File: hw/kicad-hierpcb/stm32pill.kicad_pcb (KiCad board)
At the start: 2 copper layers, 12 parts, among them U1 STM32F103C8T6

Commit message: kicad-libs/ribbon
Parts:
- moved PC 5.08 mm to (43.2, 71.1)
- moved PD 2.54 mm to (38.1, 71.1)
- moved SWD 2.54 mm to (27.9, 71.1)
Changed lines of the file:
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@@
 	(footprint "Connector_PinHeader_2.54mm:PinHeader_1x03_P2.54mm_Vertical"
 		(layer "F.Cu")
-		(at 38.1 71.12 180)
+		(at 43.18 71.12 180)
 		(descr "Through hole straight pin header, 1x03, 2.54mm pitch, single row")
 		(tags "Through hole pin header THT 1x03 2.54mm single row")
@@
 		(descr "plated through hole")
 		(property "Reference" "NRST"
-			(at -0.635 1.905 0)
+			(at -2.54 0 0)
 			(unlocked yes)
 			(layer "F.SilkS")
@@
 	(footprint "Connector_PinHeader_2.54mm:PinHeader_1x02_P2.54mm_Vertical"
 		(layer "F.Cu")
-		(at 30.48 71.12 180)
+		(at 27.94 71.12 180)
 		(descr "Through hole straight pin header, 1x02, 2.54mm pitch, single row")
 		(tags "Through hole pin header THT 1x02 2.54mm single row")
@@
 		(fp_arc
 			(start -3.379999 4.06)
-			(mid -3.394989 4.460188)
+			(mid -3.394993 4.460187)
 			(end -3.390027 4.05975)
 			(stroke
@@
 		)
 		(property "Value" "I2C_2"
-			(at 0 4.87 360)
+			(at 0 4.87 0)
 			(layer "F.Fab")
 			(effects
@@
 	(footprint "Connector_PinHeader_2.54mm:PinHeader_1x02_P2.54mm_Vertical"
 		(layer "F.Cu")
-		(at 40.64 71.12 180)
+		(at 38.1 71.12 180)
 		(descr "Through hole straight pin header, 1x02, 2.54mm pitch, single row")
 		(tags "Through hole pin header THT 1x02 2.54mm single row")

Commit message: ide stm
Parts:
- removed ADC: ADC0, base:PTH
- removed AL: Arduino Left Pins, Connector_PinHeader_2.54mm:PinHeader_1x15_P2.54mm_Vertical
- removed AR: Arduino Right Pins, Connector_PinHeader_2.54mm:PinHeader_1x15_P2.54mm_Vertical
- removed B0: Boot0, base:PTH
- removed I2C_2: I2C_2, Connector_PinHeader_2.54mm:PinHeader_1x02_P2.54mm_Vertical
- removed NRST: NRST, base:PTH
- removed PC: PC, Connector_PinHeader_2.54mm:PinHeader_1x03_P2.54mm_Vertical
- removed PD: PD, Connector_PinHeader_2.54mm:PinHeader_1x02_P2.54mm_Vertical
- removed SWD: SWD, Connector_PinHeader_2.54mm:PinHeader_1x02_P2.54mm_Vertical
- removed U1: STM32F103C8T6, jlcpcb:LQFP-48_L7.0-W7.0-P0.50-LS9.0-BL
- removed USB: USB, Connector_PinHeader_2.54mm:PinHeader_1x02_P2.54mm_Vertical
- removed Vb: VBAT, base:PTH
- added 3V3 B0 Gnd: B0 Jumper, base:3x PTH 1.7mm, F.Cu at (35.6, 61.0)
- added C1: CL21B103KBANNNC, jlcpcb:C0805, F.Cu at (42.2, 52.6)
- added C2: CL21B103KBANNNC, jlcpcb:C0805, F.Cu at (36.4, 45.0)
- added C3: CL21B103KBANNNC, jlcpcb:C0805, F.Cu at (28.6, 49.9)
- added C4: CL21B103KBANNNC, jlcpcb:C0805, F.Cu at (34.0, 58.7)
- added J1: IDE STM CD, ribbon:IDE STM CD, F.Cu at (25.4, 25.4)
- added J2: IDE STM AB, ribbon:IDE STM AB, F.Cu at (45.7, 25.4)
- added U4: STM32F103C8T6, jlcpcb:LQFP-48_L7.0-W7.0-P0.50-LS9.0-BL, F.Cu at (35.3, 51.6)
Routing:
- net +3.3V: track 0.00 -> 82.4 mm, vias 0 -> 2
- net unconnected-(J1-IDE3_STM43-PadVBusSense): track 0.00 -> 32.4 mm, vias 0 -> 2
- net unconnected-(J2-IDE4_STM22-PadB0): track 0.00 -> 23.0 mm
- net unconnected-(J1-IDE39_STM46-PadSDA): track 0.00 -> 21.2 mm
- net unconnected-(J2-IDE6_STM21-PadB1): track 0.00 -> 20.7 mm
- net unconnected-(J1-IDE5_STM25-PadC0): track 0.00 -> 19.9 mm
- net unconnected-(J1-IDE37_STM45-PadSCL): track 0.00 -> 18.8 mm
- net unconnected-(J2-IDE8_STM20-PadB2): track 0.00 -> 18.4 mm
- net unconnected-(J1-IDE7_STM26-PadC1): track 0.00 -> 17.5 mm
- net unconnected-(J1-IDE35_STM42-PadD7): track 0.00 -> 16.9 mm
- net GND: track 0.00 -> 16.6 mm, vias 0 -> 2
- net unconnected-(J2-IDE10_STM19-PadB3): track 0.00 -> 16.0 mm
- net unconnected-(J1-IDE9_STM27-PadC2): track 0.00 -> 15.2 mm
- net unconnected-(J1-IDE33_STM41-PadD6): track 0.00 -> 14.6 mm
- net unconnected-(J2-IDE12_STM18-PadB4): track 0.00 -> 13.7 mm
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
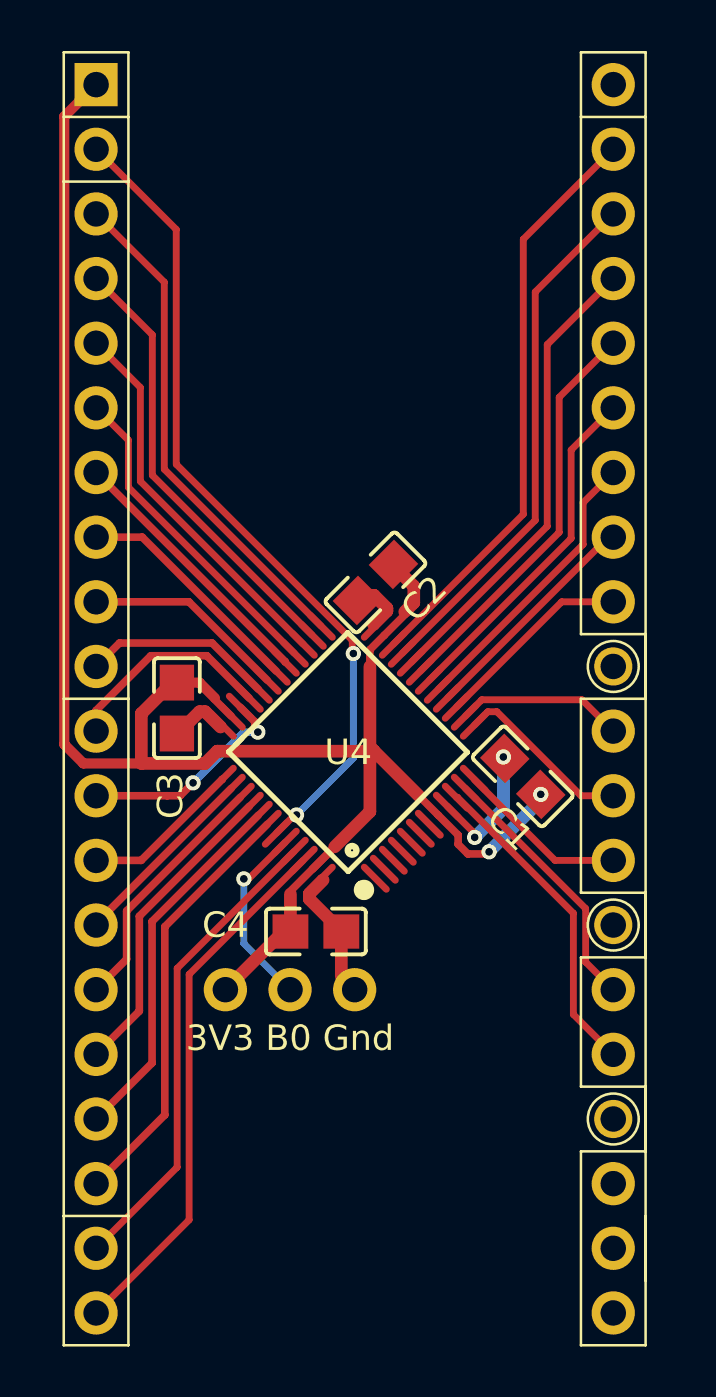
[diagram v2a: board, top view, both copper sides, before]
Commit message: stm32pill pcb
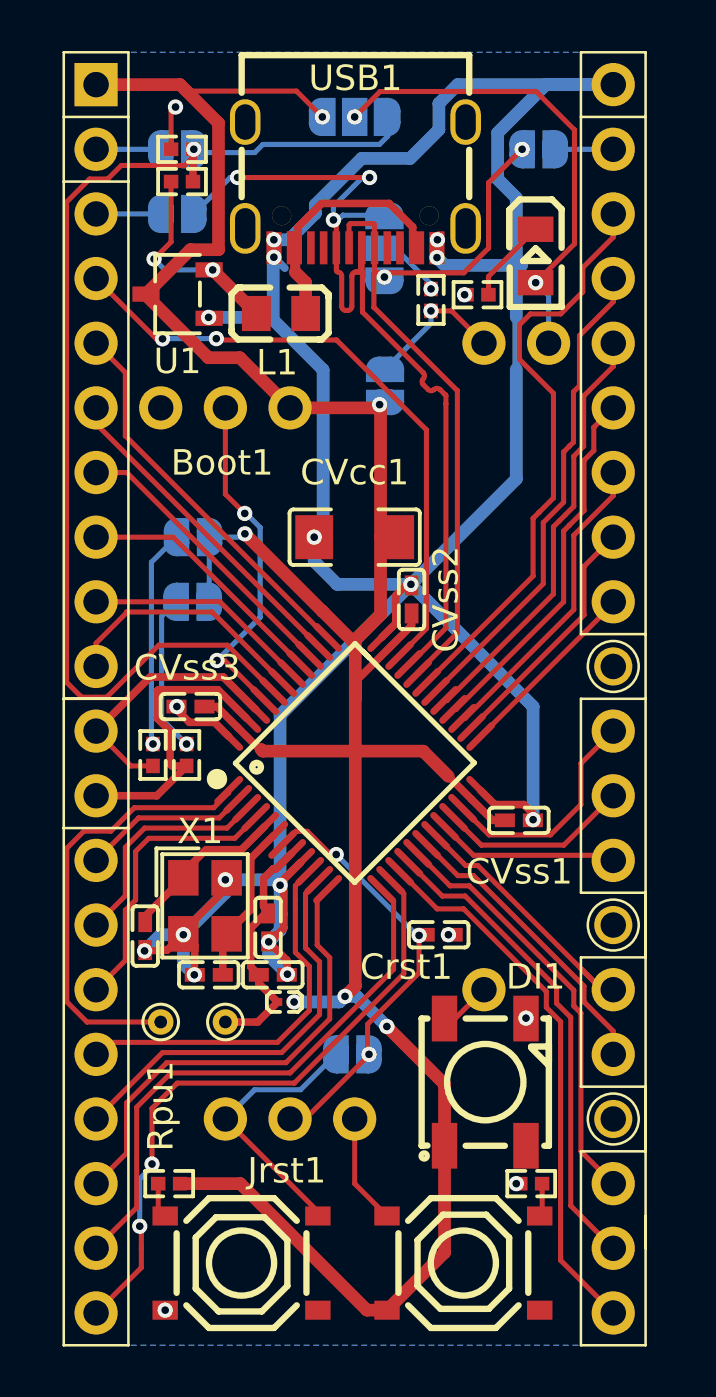
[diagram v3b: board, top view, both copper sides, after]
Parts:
- removed 3V3 B0 Gnd: B0 Jumper, base:3x PTH 1.7mm
- removed C1, C2, C3, C4: CL21B103KBANNNC, jlcpcb:C0805
- removed J1: IDE STM CD, ribbon:IDE STM CD
- removed J2: IDE STM AB, ribbon:IDE STM AB
- removed U4: STM32F103C8T6, jlcpcb:LQFP-48_L7.0-W7.0-P0.50-LS9.0-BL
- added Boot1: ~, base:3x PTH 1.7mm, F.Cu at (27.9, 38.1)
- added CVcc1: 4.7uF, jlcpcb:C1206, F.Cu at (35.6, 43.2)
- added CVss1: 100nF, jlcpcb:C0402, F.Cu at (42.0, 54.3)
- added CVss2: 100nF, jlcpcb:C0402, F.Cu at (37.8, 45.6)
- added CVss3: 100nF, jlcpcb:C0402, F.Cu at (29.1, 49.8)
- added CVssA1: 1μF, jlcpcb:C0402, F.Cu at (32.3, 60.4)
- added CVssAn1: 10nF, jlcpcb:C0402, F.Cu at (32.2, 58.5)
- added Cosc1: 30pF, jlcpcb:C0402, F.Cu at (27.3, 58.9)
- added Cosc2: 30pF, jlcpcb:C0402, F.Cu at (29.8, 60.4)
- added Crst1: 100nF, jlcpcb:C0402, F.Cu at (38.9, 58.8)
- added DI1: ~, base:PTH 1.7mm, F.Cu at (40.6, 61.0)
- added IDE_STM_A1: ~, ribbon:IDE STM A, F.Cu at (45.5, 25.4)
- added IDE_STM_B1: ~, ribbon:IDE STM B, F.Cu at (45.7, 50.8)
- added IDE_STM_C1: ~, ribbon:IDE STM C, F.Cu at (25.4, 25.4)
- added IDE_STM_D1: ~, ribbon:IDE STM D, F.Cu at (25.4, 73.7)
- added JPLed1: SolderJumper_3_Open, Jumper:SolderJumper-3_P1.3mm_Open_RoundedPad1.0x1.5mm, B.Cu at (35.6, 26.7)
- added JPResetSwitch1: SolderJumper_2_Open, Jumper:SolderJumper-2_P1.3mm_Open_RoundedPad1.0x1.5mm, B.Cu at (35.5, 63.5)
- added JPRscl1: SolderJumper_2_Open, Jumper:SolderJumper-2_P1.3mm_Open_RoundedPad1.0x1.5mm, B.Cu at (29.2, 43.2)
- added JPRsda1: SolderJumper_2_Open, Jumper:SolderJumper-2_P1.3mm_Open_RoundedPad1.0x1.5mm, B.Cu at (29.2, 45.7)
- added JPdn1: SolderJumper_2_Open, Jumper:SolderJumper-2_P1.3mm_Open_RoundedPad1.0x1.5mm, B.Cu at (42.8, 27.9)
- added JPdp1: SolderJumper_2_Open, Jumper:SolderJumper-2_P1.3mm_Open_RoundedPad1.0x1.5mm, B.Cu at (28.6, 30.5)
- added JPpuUSB1: SolderJumper_2_Open, Jumper:SolderJumper-2_P1.3mm_Open_RoundedPad1.0x1.5mm, B.Cu at (36.8, 37.2)
- added JPpuUSBpn1: SolderJumper_3_Open, Jumper:SolderJumper-3_P1.3mm_Open_RoundedPad1.0x1.5mm, B.Cu at (36.7, 31.8)
- added JPvbus1: SolderJumper_2_Open, Jumper:SolderJumper-2_P1.3mm_Open_RoundedPad1.0x1.5mm, B.Cu at (28.6, 27.9)
- added JVbat1: VBAT, TestPoint:TestPoint_THTPad_D1.0mm_Drill0.5mm, F.Cu at (27.9, 62.2)
- added Jled1: ~, base:PTH 1.7mm, F.Cu at (43.2, 35.6)
- added JpuUSB1: ~, base:PTH 1.7mm, F.Cu at (40.6, 35.6)
- added Jrst1: ~, base:PTH 1.7mm, F.Cu at (33.0, 66.0)
- added JswitchLeft1: ~, base:PTH 1.7mm, F.Cu at (30.5, 66.0)
- added JswitchRight1: ~, base:PTH 1.7mm, F.Cu at (35.6, 66.0)
- added L1: 100Ω@100MHz, jlcpcb:L0805, F.Cu at (32.7, 34.4)
- added LED1: Green, jlcpcb:LED0805-R-RD, F.Cu at (42.7, 32.1)
- added LVssA1: 18nH, jlcpcb:L0201, F.Cu at (32.8, 61.4)
- added MCU1: STM32F103C8T6, jlcpcb:LQFP-48_L7.0-W7.0-P0.50-LS9.0-BL, F.Cu at (35.6, 52.1)
- added RGB1: LED WS2812B-S XL-5050RGBC, jlcpcb:LED-SMD_4P-L5.0-W5.0-TL-1, F.Cu at (40.7, 64.6)
- added RVbusI1: 33kΩ, jlcpcb:R0402, F.Cu at (28.8, 29.2)
- added RVbusO1: 82kΩ, jlcpcb:R0402, F.Cu at (28.8, 27.9)
- added Rled1: 1k-1.5k, jlcpcb:R0402, F.Cu at (40.4, 33.7)
- added Rpd1: 10kΩ, jlcpcb:R0402, F.Cu at (42.5, 68.6)
- added Rpu1: 10kΩ, jlcpcb:R0402, F.Cu at (28.3, 68.6)
- added RpuUSB1: 1.5kΩ, jlcpcb:R0402, F.Cu at (38.6, 33.9)
- added Rscl1: 2.2kΩ, jlcpcb:R0402, F.Cu at (27.6, 51.7)
- added Rsda1: 2.2kΩ, jlcpcb:R0402, F.Cu at (29.0, 51.7)
- added SW1: Tactile Switch, jlcpcb:SW-SMD_4P-L5.1-W5.1-P3.70-LS6.5-TL_H1.5, F.Cu at (31.1, 71.7)
- added SW2: Tactile Switch, jlcpcb:SW-SMD_4P-L5.1-W5.1-P3.70-LS6.5-TL_H1.5, F.Cu at (39.8, 71.7)
- added U1: 3.3V Voltage Regulator 200mA, jlcpcb:SOT-23-3_L2.9-W1.6-P1.90-LS2.8-BR, F.Cu at (28.6, 33.6)
- added USB1: USB_C, jlcpcb:USB-C_SMD-TYPE-C-31-M-12, F.Cu at (35.6, 29.3)
- added VSSA1: VSSA, TestPoint:TestPoint_THTPad_D1.0mm_Drill0.5mm, F.Cu at (30.5, 62.2)
- added X1: Crystal 12MHz X322512MSB4SI, jlcpcb:CRYSTAL-SMD_4P-L3.2-W2.5-BL, F.Cu at (29.7, 57.7)
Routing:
- net GND: track 16.6 -> 128.6 mm, vias 2 -> 22
- net /USB VBusSense: track 0.00 -> 44.8 mm, vias 0 -> 1
- net /USBd+: track 0.00 -> 40.1 mm, vias 0 -> 3
- net unconnected-(J1-IDE3_STM43-PadVBusSense): track 32.4 -> 0.00 mm, vias 2 -> 0
- net /USBd-: track 0.00 -> 31.7 mm, vias 0 -> 2
- net +3.3V: track 82.4 -> 111.1 mm, vias 2 -> 6
- net Net-(IDE_STM_D1-IDE21_STM33): track 0.00 -> 25.2 mm, vias 0 -> 2
- net Net-(IDE_STM_C1-IDE7_STM26): track 0.00 -> 24.7 mm, vias 0 -> 2
- net /USART1 RX: track 0.00 -> 23.3 mm
- net unconnected-(J2-IDE4_STM22-PadB0): track 23.0 -> 0.00 mm
- net Net-(IDE_STM_D1-IDE23_STM34): track 0.00 -> 21.9 mm
- net /SPI1 SCK: track 0.00 -> 21.4 mm
- net unconnected-(J1-IDE39_STM46-PadSDA): track 21.2 -> 0.00 mm
- net unconnected-(J2-IDE6_STM21-PadB1): track 20.7 -> 0.00 mm
- net unconnected-(J1-IDE5_STM25-PadC0): track 19.9 -> 0.00 mm
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- added copper zone on B.Cu, net GND

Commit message: stm32-panel
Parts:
- added 3.3V1: ~, base:PTH 1.7mm, F.Cu at (43.2, 49.5)
- added G***: LOGO, base:oshw bg, F.Cu at (35.8, 50.4)
- added GND1: ~, base:PTH 1.7mm, F.Cu at (43.2, 52.2)
- added JPV1: SolderJumper_2_Open, Jumper:SolderJumper-2_P1.3mm_Open_RoundedPad1.0x1.5mm, B.Cu at (28.6, 25.4)
- added RpuBoot1: 33kΩ, jlcpcb:R0402, F.Cu at (31.8, 39.5)
- IDE_STM_B1: footprint ribbon:IDE STM B -> ribbon:IDE STM B cut
- IDE_STM_D1: footprint ribbon:IDE STM D -> ribbon:IDE STM D cut
- moved IDE_STM_D1 22.0 mm to (25.4, 51.6), turned to 0 degrees
- moved DI1 10.2 mm to (35.6, 69.8)
- moved Rpd1 2.58 mm to (40.6, 66.8)
- moved RGB1 1.69 mm to (40.7, 62.9)
- moved SW2 1.60 mm to (39.8, 70.1)
- moved SW1 1.60 mm to (31.1, 70.1)
- moved Rpu1 1.33 mm to (28.2, 67.2)
- renumbered JPResetSwitch1 to JPReset1, JPpuUSBpn1 to JPpuUSB1, JPpuUSB1 to JPpuUSBconst1, JswitchRight1 to JSH1, JswitchLeft1 to JSL1
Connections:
- IDE_STM_C1 pad 3V3: +3.3V -> Net-(IDE_STM_C1-IDE1_STM23)
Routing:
- net GND: track 128.6 -> 147.2 mm
- net Net-(DI1-Pin_1): track 2.02 -> 11.6 mm, vias 0 -> 2
- net Net-(IDE_STM_C1-IDE1_STM23): track 0.00 -> 2.51 mm, vias 0 -> 1
- net +3.3V: track 111.1 -> 113.4 mm, vias 6 -> 7
- net /Boot0: track 13.8 -> 15.5 mm
- net Net-(JSH1-Pin_1): track 4.34 -> 2.72 mm
- net Net-(IDE_STM_D1-IDE21_STM33): track 25.2 -> 23.9 mm
- net /SPI1 MISO: track 19.0 -> 20.1 mm
- net Net-(SW2-C): track 1.31 -> 2.34 mm
- net /SPI1 SCK: track 21.4 -> 22.2 mm, vias 0 -> 1
- net Net-(JPReset1-B): track 11.2 -> 10.5 mm
- net Net-(IDE_STM_B1-IDE32_STM10): track 11.6 -> 12.3 mm
- net /SPI1 MOSI: track 16.6 -> 17.2 mm
- net Net-(IDE_STM_B1-IDE30_STM11): track 10.6 -> 10.0 mm
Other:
- board outline added: 23.1 x 49 mm
- board text added: "A"
- board text added: "B"
- board text added: "C"
- board text added: "D"
- board text added: "Flash UART"
- board text added: "SCL"
- board text added: "SDA"
- board text added: "TX RX"
- board text added: "https://github.com/johannesloetzsch/pillbus"

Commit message: bus
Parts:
- LVssA1: value 18nH -> 15-30nH; footprint jlcpcb:L0201 -> jlcpcb:L0402
- RVbusI1, RpuBoot1: value 33kΩ -> 51kΩ
- RVbusO1: value 82kΩ -> 100kΩ
- moved LVssA1 0.48 mm to (32.3, 61.5)
- moved Crst1 0.06 mm to (38.8, 58.8)
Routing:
- net /USB VBusSense: track 44.8 -> 37.3 mm, vias 1 -> 2
- net /VSSA: track 9.50 -> 8.56 mm
- net Net-(IDE_STM_C1-IDE5_STM25): vias 0 -> 1
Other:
- board size 23.1 x 49 mm -> 23.8 x 49 mm

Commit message: improved layout
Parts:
- removed VSSA1: VSSA, TestPoint:TestPoint_THTPad_D1.0mm_Drill0.5mm
- added CC1_1: ~, base:TestPoint_THTPad_D1.0mm_Drill0.5mm, F.Cu at (41.3, 25.4)
- added CC2_1: ~, base:TestPoint_THTPad_D1.0mm_Drill0.5mm, F.Cu at (27.9, 25.4)
- added CLed1: 100nF, jlcpcb:C0402, F.Cu at (34.2, 58.3)
- added CUin1: 1μF, jlcpcb:C0402, F.Cu at (31.9, 34.1)
- added CUout1: 1μF, jlcpcb:C0402, F.Cu at (29.6, 30.8)
- added DO1: ~, base:PTH 1.7mm, F.Cu at (33.0, 66.0)
- added RGB2: LED WS2812B, jlcpcb:LED-SMD_4P-L5.0-W5.0-TL-1, F.Cu at (40.4, 61.6)
- added SBU1_1: ~, base:TestPoint_THTPad_D1.0mm_Drill0.5mm, F.Cu at (29.8, 25.4)
- added SBU2_1: ~, base:TestPoint_THTPad_D1.0mm_Drill0.5mm, F.Cu at (43.2, 25.4)
- JPV1: value SolderJumper_2_Open -> SolderJumper_3_Open; footprint Jumper:SolderJumper-2_P1.3mm_Open_RoundedPad1.0x1.5mm -> Jumper:SolderJumper-3_P1.3mm_Open_RoundedPad1.0x1.5mm
- JVbat1: footprint TestPoint:TestPoint_THTPad_D1.0mm_Drill0.5mm -> base:TestPoint_THTPad_D1.0mm_Drill0.5mm
- RGB1: value LED WS2812B-S XL-5050RGBC -> LED WS2812B
- moved CVcc1 18.3 mm to (35.6, 61.5), turned to -90 degrees
- moved JVbat1 14.2 mm to (30.5, 48.3)
- moved CVss2 11.8 mm to (39.0, 42.9), turned to 0 degrees
- moved Crst1 10.6 mm to (35.5, 68.9), turned to 90 degrees
- moved RGB1 10.5 mm to (30.3, 61.5), turned to 180 degrees
- moved JPpuUSBconst1 9.89 mm to (31.4, 28.9), turned to 180 degrees
- moved JPV1 8.97 mm to (29.2, 34.4), turned to 180 degrees
- moved JPdn1 8.89 mm to (36.6, 34.4)
- moved CVss1 7.62 mm to (43.6, 50.5)
- moved Boot1 7.62 mm to (35.6, 38.1), turned to 180 degrees
- moved LVssA1 7.43 mm to (37.6, 56.3)
- moved Cosc1 7.32 mm to (30.3, 52.1), turned to 45 degrees
- moved Rled1 7.20 mm to (43.2, 27.0), turned to 180 degrees
- moved JPReset1 6.35 mm to (35.6, 69.8)
- moved DI1 6.35 mm to (30.5, 66.0)
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- renumbered CVss2 to CVss1, CVss1 to CVss2
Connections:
- CVcc1 pad 1: GND -> +3.3V
- CVcc1 pad 2: +3.3V -> GND
- IDE_STM_D1 pad SCL: /I2C1 SDA -> /I2C1 SCL
- IDE_STM_D1 pad SDA: /I2C1 SCL -> /I2C1 SDA
- JPV1 pad 1: Net-(IDE_STM_C1-IDE1_STM23) -> Net-(JPV1-A)
- RGB1 pad 2: unconnected-(RGB1-DO-Pad2) -> Net-(RGB1-DO)
- U1 pad 3: +3.3V -> Net-(JPV1-A)
- USB1 pad A5: unconnected-(USB1-CC1-PadA5) -> /CC1
- USB1 pad A8: unconnected-(USB1-SBU1-PadA8) -> /SBU1
- USB1 pad B5: unconnected-(USB1-CC2-PadB5) -> /CC2
- USB1 pad B8: unconnected-(USB1-SBU2-PadB8) -> /SBU2
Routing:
- net GND: track 147.3 -> 45.8 mm, vias 22 -> 20
- net Net-(JPpuUSBconst1-A): track 5.65 -> 20.4 mm, vias 1 -> 2
- net /VBAT: track 17.4 -> 3.52 mm
- net Net-(IDE_STM_A1-IDE4_STM22): track 2.57 -> 14.8 mm, vias 0 -> 1
- net /NRST: track 17.2 -> 29.4 mm, vias 3 -> 2
- net Net-(RGB1-DO): track 0.00 -> 11.3 mm, vias 0 -> 4
- net /CC2: track 0.00 -> 10.7 mm
- net /SBU2: track 0.00 -> 10.6 mm
- net /SBU1: track 0.00 -> 10.5 mm
- net Net-(IDE_STM_C1-IDE1_STM23): track 2.51 -> 12.2 mm, vias 1 -> 0
- net /CC1: track 0.00 -> 9.08 mm
- net Net-(IDE_STM_C1-IDE5_STM25): track 2.54 -> 11.4 mm, vias 1 -> 0
- net /USBd+: track 40.1 -> 33.5 mm, vias 3 -> 1
- net Net-(DI1-Pin_1): track 11.6 -> 5.15 mm, vias 2 -> 1
- net Net-(JPpuUSB1-C): track 2.61 -> 8.97 mm
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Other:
- board text added: "3V3"
- board text added: ">"
- board text added: "Flash"
- board text added: "Gnd"
- board text added: "I2C"
- board text added: "LED"
- board text added: "RX"
- board text added: "Resetswitch"
- board text added: "TX"
- board text added: "UART"
- board text added: "USB"
- board text added: "USBpu"
- board text added: "Vcc"
- board text removed: "Flash UART"
- board text removed: "TX RX"

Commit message: annotations
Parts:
- added VBus_1: ~, base:TestPoint_THTPad_D1.0mm_Drill0.5mm, F.Cu at (40.6, 33.7)
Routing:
- net Net-(VBus_1-Pin_1): track 13.8 -> 17.8 mm
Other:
- board text added: "3V3 Gnd"
- board text added: "HS"
- board text added: "Ide"
- board text added: "LS"
- board text added: "Reset@SwitchL"
- board text added: "VBus"
- board text added: "v0.1.0"
- board text removed: "Resetswitch"

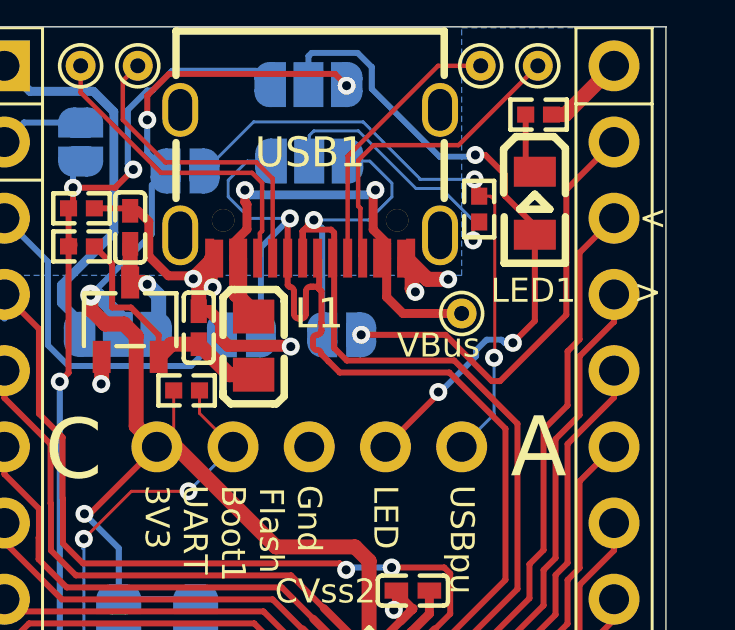
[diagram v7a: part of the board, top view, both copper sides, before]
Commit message: changed layout of bus board
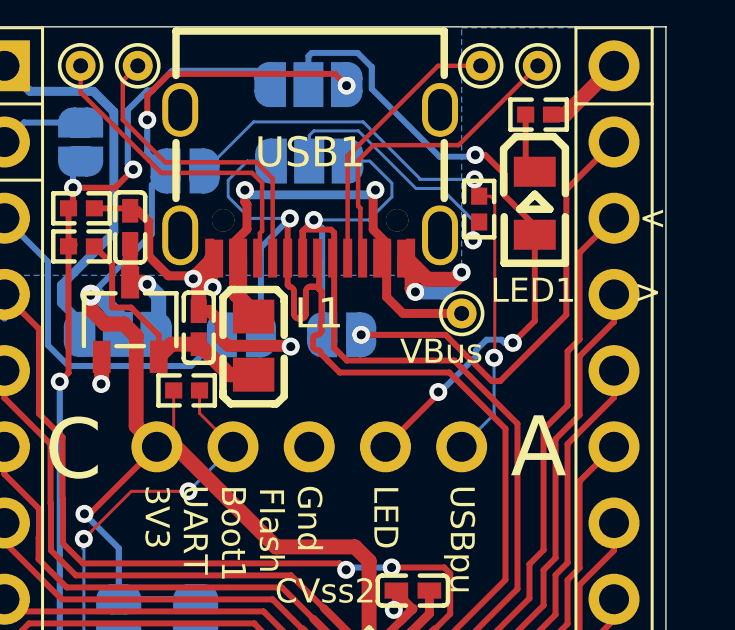
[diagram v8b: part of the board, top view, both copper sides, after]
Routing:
- net GND: track 45.8 -> 48.1 mm
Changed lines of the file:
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@@
 	)
 	(gr_text "VBus\n"
-		(at 38.481 34.7218 0)
+		(at 38.5826 34.925 0)
 		(layer "F.SilkS")
 		(effects
@@
 	)
 	(segment
+		(start 38.87 31.884924)
+		(end 39.501126 32.51605)
+		(width 0.5)
+		(layer "F.Cu")
+		(net 2)
+	)
+	(segment
 		(start 32.591453 47.80114)
 		(end 31.866913 47.0766)
@@
 	)
 	(segment
-		(start 40.191182 32.51605)
-		(end 39.501126 32.51605)
-		(width 0.5)
-		(layer "F.Cu")
-		(net 2)
-	)
-	(segment
 		(start 30.345742 54.514635)
 		(end 30.345742 55.61744)
@@
 	)
 	(segment
+		(start 39.501126 32.51605)
+		(end 40.40735 32.51605)
+		(width 0.5)
+		(layer "F.Cu")
+		(net 2)
+	)
+	(segment
 		(start 31.694924 32.441421)
 		(end 31.653503 32.4)
@@
 	)
 	(segment
+		(start 40.40735 32.51605)
+		(end 40.64 32.2834)
+		(width 0.5)
+		(layer "F.Cu")
+		(net 2)
+	)
+	(segment
 		(start 30.345742 52.99296)
 		(end 29.887891 52.535109)
@@
 		(end 29.591 30.2348)
 		(width 0.3)
-		(layer "F.Cu")
-		(net 2)
-	)
-	(segment
-		(start 39.501126 32.51605)
-		(end 38.87 31.884924)
-		(width 0.5)
 		(layer "F.Cu")
 		(net 2)
@@
 	)
 	(via
-		(at 40.191182 32.51605)
-		(size 0.6)
-		(drill 0.3)
-		(layers "F.Cu" "B.Cu")
-		(net 2)
-	)
+		(at 40.64 32.2834)
+		(size 0.6)
+		(drill 0.3)
+		(layers "F.Cu" "B.Cu")
+		(net 2)
+	)
+	(segment
+		(start 39.986043 32.937357)
+		(end 39.097043 32.937357)
+		(width 0.5)
+		(layer "B.Cu")
+		(net 2)
+	)
+	(segment
+		(start 40.64 32.2834)
+		(end 39.986043 32.937357)
+		(width 0.5)
+		(layer "B.Cu")
+		(net 2)
+	)
